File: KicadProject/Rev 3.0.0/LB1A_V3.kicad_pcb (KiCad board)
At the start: 6 copper layers, 45 x 45 mm, 194 parts, among them J601 2337019-1, J602 2337019-1, U101 LFBGA448_18X18, U201 AS4C256M16D3LC-12BCN, U401 STPMIC1xPQR, U501 S40FC004C1B2C00000, U601 LBEE59B1LV-278, U701 DF40C-100DP-0.4V(51), U702 DF40C-100DP-0.4V(51), U703 DF40C-100DP-0.4V(51), X101 32.768kHz, Y101 24MHz

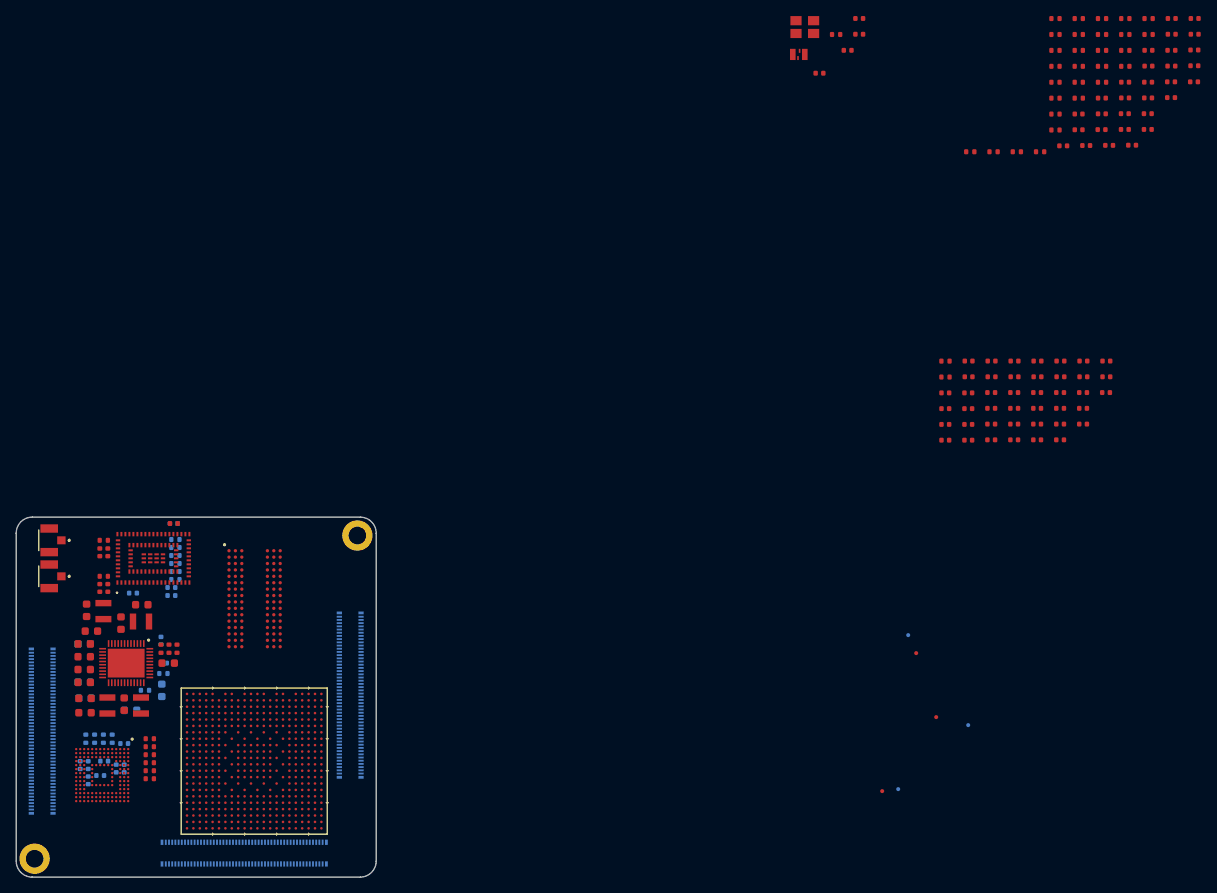
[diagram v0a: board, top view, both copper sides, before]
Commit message: working on mpu placement
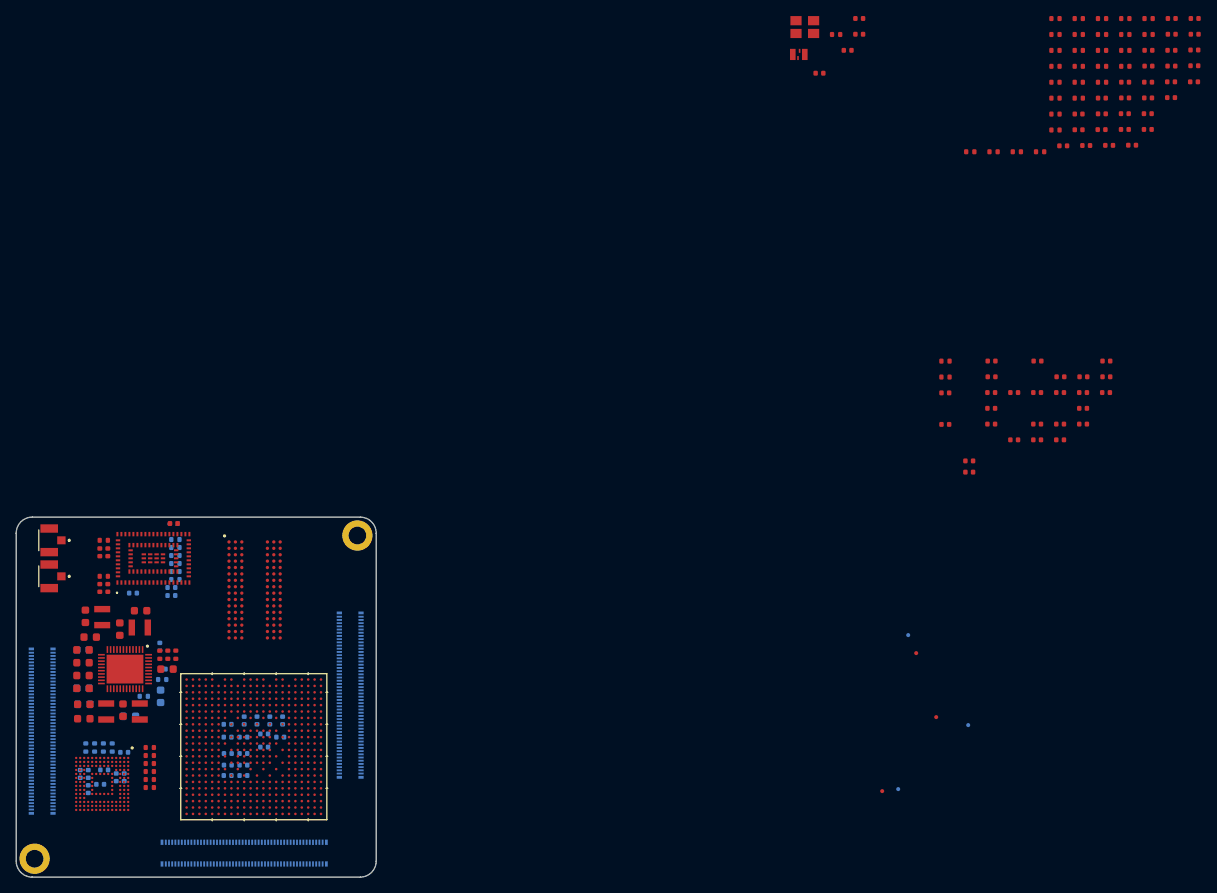
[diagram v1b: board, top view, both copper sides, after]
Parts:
- C305, C306, C307, C308, C313, C314, C315, C316, C321, C322, C323, C324, C326, C327, C328, C329: moved to B.Cu
- moved C307 117.7 mm to (126.5, 114.5), turned to 180 degrees
- moved C314 111.5 mm to (128.5, 110.4), turned to 90 degrees
- moved C305 111.1 mm to (126.4, 117.3), turned to 180 degrees
- moved C322 108.5 mm to (128.4, 117.3), turned to 180 degrees
- moved C327 107.5 mm to (131.0, 112.1)
- moved C326 107.2 mm to (128.4, 112.5), turned to 180 degrees
- moved C306 107.1 mm to (126.5, 116.0), turned to 180 degrees
- moved C313 106.0 mm to (126.4, 110.9), turned to 180 degrees
- moved C316 105.1 mm to (131.7, 110.4), turned to 90 degrees
- moved C323 103.8 mm to (128.4, 116.0), turned to 180 degrees
- moved C308 102.4 mm to (126.4, 112.5), turned to 180 degrees
- moved C324 100.3 mm to (128.4, 114.5), turned to 180 degrees
- moved C328 98.5 mm to (131.0, 113.8)
- moved C315 95.6 mm to (130.1, 110.4), turned to 90 degrees
- moved C329 92.7 mm to (133.0, 112.5)
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
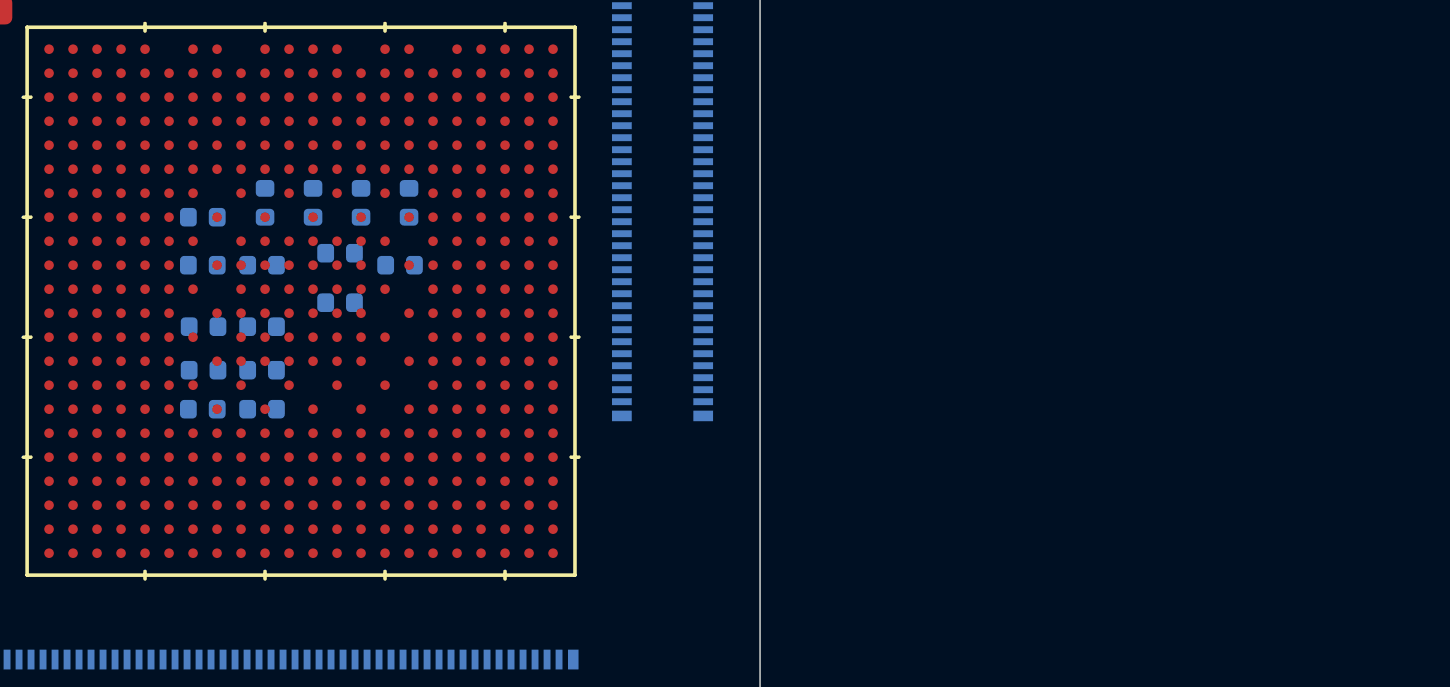
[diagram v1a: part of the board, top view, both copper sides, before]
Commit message: working on mpu placements
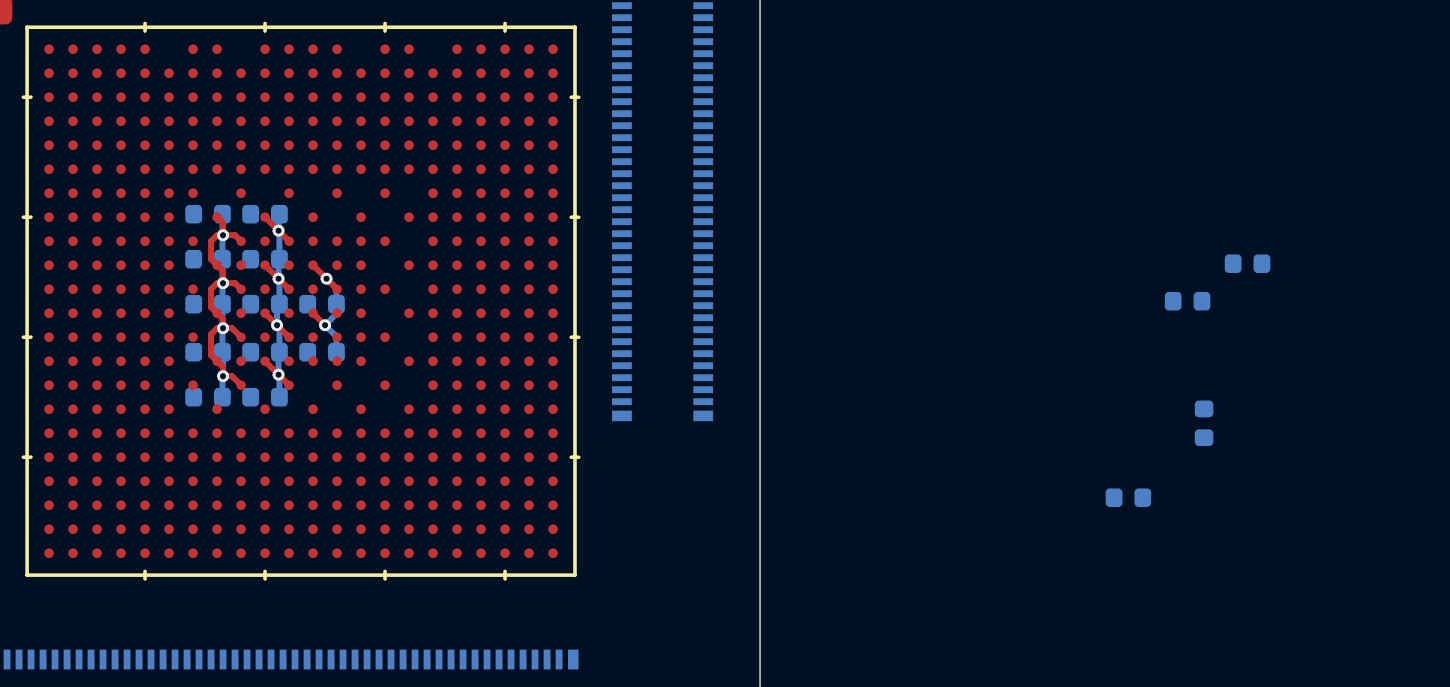
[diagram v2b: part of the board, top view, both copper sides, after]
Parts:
- moved C326 29.9 mm to (157.3, 120.2), turned to 0 degrees
- moved C327 29.4 mm to (159.8, 117.8), turned to 90 degrees
- moved C328 28.3 mm to (159.2, 113.7)
- moved C329 28.3 mm to (161.2, 112.5)
- moved C322 6.50 mm to (128.5, 110.8)
- moved C314 6.48 mm to (128.5, 116.9), turned to 180 degrees
- moved C315 5.23 mm to (128.5, 115.4), turned to 180 degrees
- moved C321 5.16 mm to (128.5, 112.3), turned to 180 degrees
- moved C316 4.65 mm to (128.5, 113.8), turned to 180 degrees
- moved C324 2.14 mm to (130.4, 113.8)
- moved C323 2.09 mm to (130.4, 115.4)
- moved C307 0.76 mm to (126.6, 113.8)
- moved C306 0.62 mm to (126.6, 115.4)
- moved C305 0.44 mm to (126.6, 116.9)
- moved C308 0.27 mm to (126.6, 112.3)
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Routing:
- net PMIC_VOUT1_VDD_CORE: track 0.00 -> 31.1 mm, vias 0 -> 10
